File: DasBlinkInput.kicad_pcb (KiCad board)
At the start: 4 copper layers, 25.4 x 50.8 mm, 34 parts, among them P101 CONN_01X02, P102 CONN_01X01, P103 CONN_01X01, P104 CONN_01X01, P105 CONN_01X05, P201 CONN_01X01, P301 CONN_01X01, P401 CONN_01X01, P501 CONN_01X01, U101 LP2980IM5-3.0/NOPB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

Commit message: Start of connecting the layout
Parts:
- P101: value CONN_01X02 -> Vin
- P102: value CONN_01X01 -> VGND
- P103: value CONN_01X01 -> 3V
- P104: value CONN_01X01 -> GND
- P105: value CONN_01X05 -> Output
- P201: value CONN_01X01 -> Sig1
- P301: value CONN_01X01 -> Sig2
- P401: value CONN_01X01 -> Sig3
- P501: value CONN_01X01 -> Sig4
- moved RV201 19.2 mm to (112.5, 124.6)
- moved R101 7.64 mm to (88.4, 94.2), turned to 180 degrees
- moved R103 7.45 mm to (91.2, 87.2), turned to 90 degrees
- moved P104 4.59 mm to (105.0, 111.0)
- moved C202 4.06 mm to (96.5, 109.5)
- moved C101 1.91 mm to (96.8, 89.4)
- moved P105 1.09 mm to (88.6, 132.7), turned to 90 degrees
- moved R102 1.05 mm to (88.4, 96.5)
- moved P101 0.89 mm to (95.5, 86.4)
- moved C102 0.57 mm to (99.3, 93.0)
- moved U101 0.25 mm to (96.5, 90.4)
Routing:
- net VGND: track 0.00 -> 24.8 mm, vias 0 -> 6
- net GND: track 0.00 -> 15.8 mm, vias 0 -> 2
- net 3V: track 0.00 -> 12.5 mm, vias 0 -> 5
- net Net-(R103-Pad1): track 0.00 -> 4.68 mm
- net Net-(C101-Pad1): track 1.94 -> 6.26 mm
- added copper zone on GND.Cu, net VGND
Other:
- net class Default: clearance 0.1524 -> 0.254
- rule trace_clearance: 0.1524 -> 0.254

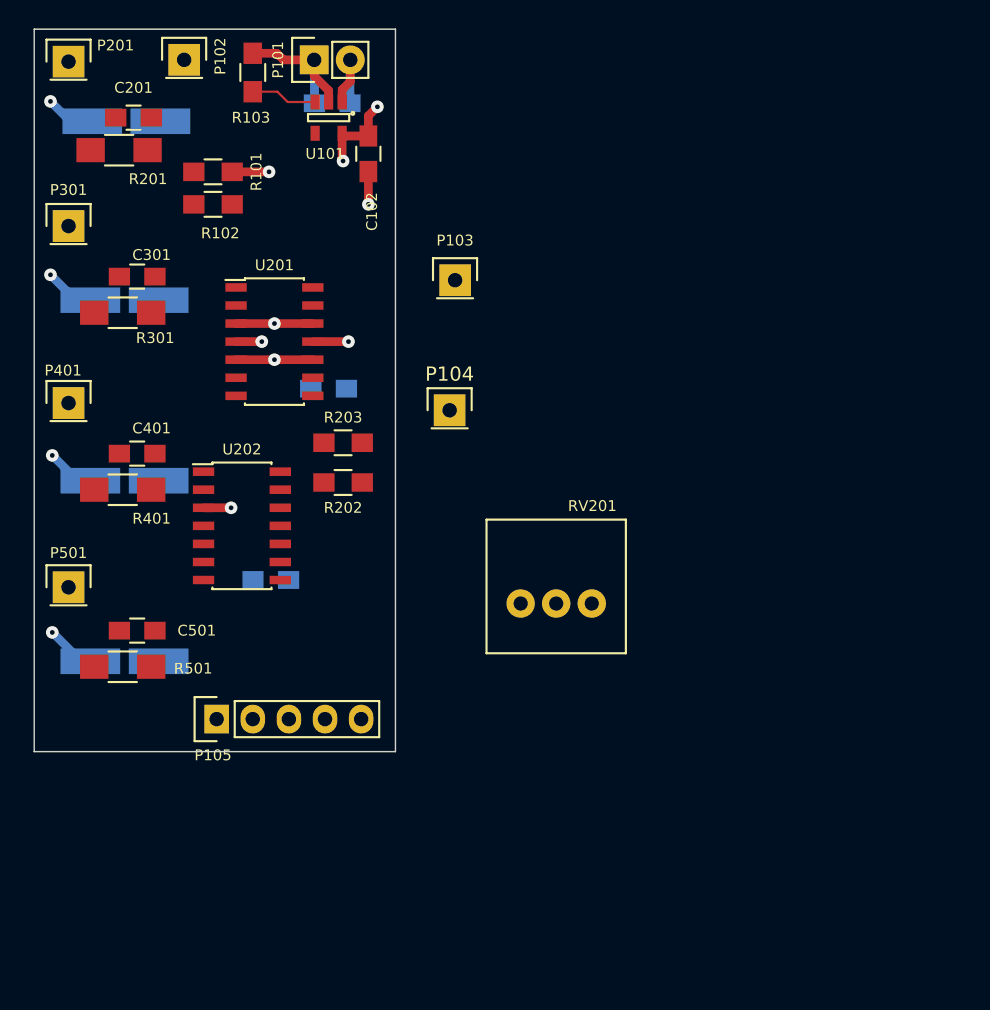
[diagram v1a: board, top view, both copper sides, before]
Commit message: Commencting new layout on corrected iPod defintion
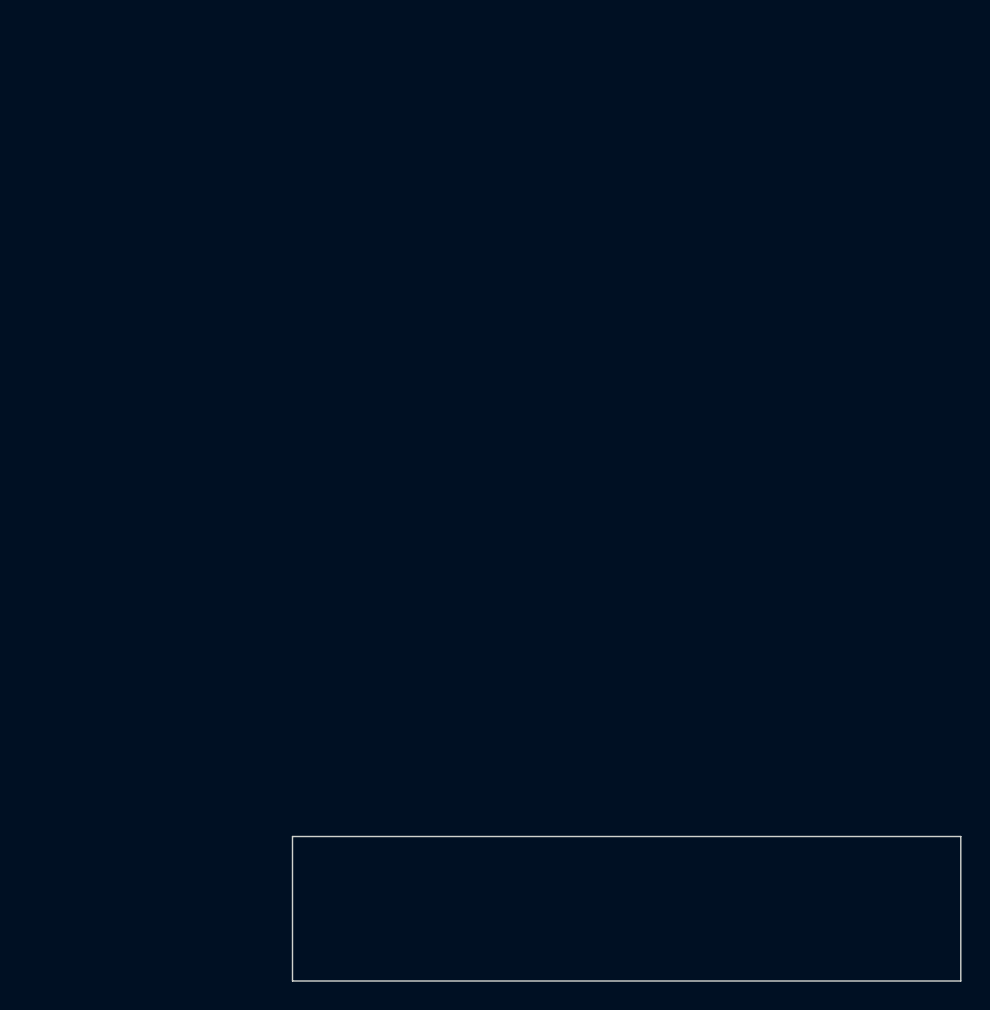
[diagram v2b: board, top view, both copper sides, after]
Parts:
- removed C101, C102: 1U, Capacitors_SMD:C_0805_HandSoldering
- removed C201, C301, C401, C501: 100p, Capacitors_SMD:C_0805_HandSoldering
- removed C202, C203: 0.1U, Capacitors_SMD:C_0805_HandSoldering
- removed P101: Vin, Pin_Headers:Pin_Header_Straight_1x02
- removed P102: VGND, Pin_Headers:Pin_Header_Straight_1x01
- removed P103: 3V, Pin_Headers:Pin_Header_Straight_1x01
- removed P104: GND, Pin_Headers:Pin_Header_Straight_1x01
- removed P105: Output, Pin_Headers:Pin_Header_Straight_1x05
- removed P201: Sig1, Pin_Headers:Pin_Header_Straight_1x01
- removed P301: Sig2, Pin_Headers:Pin_Header_Straight_1x01
- removed P401: Sig3, Pin_Headers:Pin_Header_Straight_1x01
- removed P501: Sig4, Pin_Headers:Pin_Header_Straight_1x01
- removed PD201, PD301, PD401, PD501: VBPW34SR, DasBlinkInput:VBPW34SR*
- removed R101, R102, R202, R203: 10K, Resistors_SMD:R_0805_HandSoldering
- removed R103: 0, Resistors_SMD:R_0805_HandSoldering
- removed R201, R301, R401, R501: 1MEG, Resistors_SMD:R_1206_HandSoldering
- removed RV201: POT, DasBlinkInput:P090L-02F25BR10K
- removed U101: LP2980IM5-3.0/NOPB, Housings_SOT-23_SOT-143_TSOT-6:SOT-23-5
- removed U201: MCP6404, Housings_SOIC:SOIC-14_3.9x8.7mm_Pitch1.27mm
- removed U202: LM339, Housings_SOIC:SOIC-14_3.9x8.7mm_Pitch1.27mm
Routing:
- net VGND: track 24.8 -> 0.00 mm, vias 6 -> 0
- net GND: track 15.8 -> 0.00 mm, vias 2 -> 0
- net 3V: track 12.5 -> 0.00 mm, vias 5 -> 0
- net Net-(C101-Pad1): track 6.26 -> 0.00 mm
- net Net-(R103-Pad1): track 4.68 -> 0.00 mm
- removed copper zone on PWR.Cu, net 3V
- removed copper zone on GND.Cu, net GND
- removed copper zone on GND.Cu, net VGND
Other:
- board size 25.4 x 50.8 mm -> 47 x 10.2 mm
- copper layers 4 -> 2
- net class Default: clearance 0.254 -> 0.2; trace_width 0.1524 -> 0.25; via_dia 0.6858 -> 0.6; via_drill 0.3302 -> 0.4
- net class Power removed
- rule trace_clearance: 0.254 -> 0.2
- rule trace_min: 0.1524 -> 0.2
- rule via_min_drill: 0.3302 -> 0.3
- rule via_min_size: 0.6858 -> 0.4
